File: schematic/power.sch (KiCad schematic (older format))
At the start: 21 parts, among them J1 Conn_01x02, J2 Conn_01x02, J3 Conn_01x02, J4 Conn_01x02, J5 Conn_02x06_Odd_Even, U1 LM2595S-3.3, U2 INA219AxD

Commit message: correct power D1, C1, C2 and L1 footprint. accurate L1, D1 and C2 values
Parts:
- D1: footprint Diode_SMD:D_0805_2012Metric_Castellated -> Diode_THT:D_DO-201AD_P15.24mm_Horizontal
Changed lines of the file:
@@
 F 0 "D1" V 5954 4679 50  0000 L CNN
 F 1 "D" V 6045 4679 50  0000 L CNN
-F 2 "Diode_SMD:D_0805_2012Metric_Castellated" H 6000 4600 50  0001 C CNN
+F 2 "Diode_THT:D_DO-201AD_P15.24mm_Horizontal" H 6000 4600 50  0001 C CNN
 F 3 "~" H 6000 4600 50  0001 C CNN
 	1    6000 4600

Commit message: added version
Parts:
- removed C1: C680uF, Capacitor_SMD:C_0805_2012Metric_Pad1.15x1.40mm_HandSolder, symbol Device:C
- removed C2: C220uF, Capacitor_SMD:C_0805_2012Metric_Pad1.15x1.40mm_HandSolder, symbol Device:C
- added C1, C2: 220uF, Capacitor_THT:CP_Radial_D8.0mm_P5.00mm, symbol Device:CP
- D1: value D -> 1N5822
- L1: value L33uH -> 68uH; footprint Inductor_SMD:L_1206_3216Metric_Pad1.42x1.75mm_HandSolder -> Inductor_SMD:L_Wuerth_WE-PD-Typ-7345
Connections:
- net +12V: now also C1.1
- net +3V3: now also C2.1
- net GND: now also C1.2, C2.2
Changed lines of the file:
@@
-	1    0    0    -1
-$EndComp
-$Comp
-L Device:C C2
-U 1 1 5EEDDF18
-P 6600 4600
-AR Path="/5EEDDF18" Ref="C2"  Part="1"
-AR Path="/5EEC6D97/5EEDDF18" Ref="C5"  Part="1"
-F 0 "C2" H 6715 4646 50  0000 L CNN
-F 1 "C220uF" H 6715 4555 50  0000 L CNN
-F 2 "Capacitor_SMD:C_0805_2012Metric_Pad1.15x1.40mm_HandSolder" H 6638 4450 50  0001 C CNN
-F 3 "~" H 6600 4600 50  0001 C CNN
-	1    6600 4600
-	1    0    0    -1
-$EndComp
-$Comp
-L Device:C C1
-U 1 1 5EEDDF1E
-P 4150 4400
-AR Path="/5EEDDF1E" Ref="C1"  Part="1"
-AR Path="/5EEC6D97/5EEDDF1E" Ref="C4"  Part="1"
-F 0 "C1" H 4265 4446 50  0000 L CNN
-F 1 "C680uF" H 4265 4355 50  0000 L CNN
-F 2 "Capacitor_SMD:C_0805_2012Metric_Pad1.15x1.40mm_HandSolder" H 4188 4250 50  0001 C CNN
-F 3 "~" H 4150 4400 50  0001 C CNN
-	1    4150 4400
 	1    0    0    -1
 $EndComp
@@
 AR Path="/5EEC6D97/5EEDDF32" Ref="D1"  Part="1"
 F 0 "D1" V 5954 4679 50  0000 L CNN
-F 1 "D" V 6045 4679 50  0000 L CNN
+F 1 "1N5822" V 6045 4679 50  0000 L CNN
 F 2 "Diode_THT:D_DO-201AD_P15.24mm_Horizontal" H 6000 4600 50  0001 C CNN
 F 3 "~" H 6000 4600 50  0001 C CNN
@@
 AR Path="/5EEC6D97/5EEDDF38" Ref="L1"  Part="1"
 F 0 "L1" V 6440 4450 50  0000 C CNN
-F 1 "L33uH" V 6349 4450 50  0000 C CNN
-F 2 "Inductor_SMD:L_1206_3216Metric_Pad1.42x1.75mm_HandSolder" H 6250 4450 50  0001 C CNN
+F 1 "68uH" V 6349 4450 50  0000 C CNN
+F 2 "Inductor_SMD:L_Wuerth_WE-PD-Typ-7345" H 6250 4450 50  0001 C CNN
 F 3 "~" H 6250 4450 50  0001 C CNN
 	1    6250 4450
@@
 Wire Wire Line
 	3600 4550 4150 4550
-Connection ~ 4150 4550
 $Comp
 L Connector_Generic:Conn_01x02 J1
@@
 Wire Wire Line
 	3400 4250 4150 4250
+$Comp
+L Device:CP C2
+U 1 1 5F0E578E
+P 6600 4600
+F 0 "C2" H 6718 4646 50  0000 L CNN
+F 1 "220uF" H 6718 4555 50  0000 L CNN
+F 2 "Capacitor_THT:CP_Radial_D8.0mm_P5.00mm" H 6638 4450 50  0001 C CNN
+F 3 "https://datasheet.octopart.com/EEUFM1V221L-Panasonic-datasheet-13266715.pdf" H 6600 4600 50  0001 C CNN
+F 4 "35" H 6600 4600 50  0001 C CNN "volt"
+	1    6600 4600
+	1    0    0    -1
+$EndComp
+$Comp
+L Device:CP C1
+U 1 1 5F0ECFE3
+P 4150 4400
+F 0 "C1" H 4268 4446 50  0000 L CNN
+F 1 "220uF" H 4268 4355 50  0000 L CNN
+F 2 "Capacitor_THT:CP_Radial_D8.0mm_P5.00mm" H 4188 4250 50  0001 C CNN
+F 3 "~" H 4150 4400 50  0001 C CNN
+	1    4150 4400
+	1    0    0    -1
+$EndComp
+Connection ~ 4150 4550
 $EndSCHEMATC

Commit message: added MPN
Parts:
- C3: MPN (none) -> C0805C106K8PACTU
- C4, C5: MPN (none) -> C0805C104J5RACTU
- D1: MPN (none) -> 1N5822
- L1: footprint Inductor_SMD:L_Wuerth_WE-PD-Typ-7345 -> Inductor_THT:L_Radial_L16.1mm_W16.1mm_Px7.62mm_Py12.70mm_Pulse_LP-44; MPN (none) -> PE-53830NL
- R1, R3: MPN (none) -> ERJ-P06J100V
- R2: footprint Resistor_SMD:R_4020_10251Metric_Pad1.65x5.30mm_HandSolder -> Resistor_SMD:R_2512_6332Metric_Pad1.52x3.35mm_HandSolder; MPN (none) -> CSNL2512FT1L00
- R4, R5: MPN (none) -> ERA-6AEB103V
- U2: MPN (none) -> INA219AIDR
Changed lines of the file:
@@
 F 2 "Diode_THT:D_DO-201AD_P15.24mm_Horizontal" H 6000 4600 50  0001 C CNN
 F 3 "~" H 6000 4600 50  0001 C CNN
+F 4 "1N5822" V 6000 4600 50  0001 C CNN "MPN"
 	1    6000 4600
 	0    1    1    0
@@
 F 0 "L1" V 6440 4450 50  0000 C CNN
 F 1 "68uH" V 6349 4450 50  0000 C CNN
-F 2 "Inductor_SMD:L_Wuerth_WE-PD-Typ-7345" H 6250 4450 50  0001 C CNN
+F 2 "Inductor_THT:L_Radial_L16.1mm_W16.1mm_Px7.62mm_Py12.70mm_Pulse_LP-44" H 6250 4450 50  0001 C CNN
 F 3 "~" H 6250 4450 50  0001 C CNN
+F 4 "PE-53830NL " V 6250 4450 50  0001 C CNN "MPN"
 	1    6250 4450
 	0    -1   -1   0
@@
 F 0 "R2" V 3043 4000 50  0000 C CNN
 F 1 "1m" V 3134 4000 50  0000 C CNN
-F 2 "Resistor_SMD:R_4020_10251Metric_Pad1.65x5.30mm_HandSolder" V 3180 4000 50  0001 C CNN
+F 2 "Resistor_SMD:R_2512_6332Metric_Pad1.52x3.35mm_HandSolder" V 3180 4000 50  0001 C CNN
 F 3 "~" H 3250 4000 50  0001 C CNN
+F 4 "CSNL2512FT1L00" V 3250 4000 50  0001 C CNN "MPN"
 	1    3250 4000
 	0    1    1    0
@@
 F 2 "Capacitor_SMD:C_0805_2012Metric_Pad1.15x1.40mm_HandSolder" H 3288 3450 50  0001 C CNN
 F 3 "~" H 3250 3600 50  0001 C CNN
+F 4 "C0805C104J5RACTU" V 3250 3600 50  0001 C CNN "MPN"
 	1    3250 3600
 	0    1    1    0
@@
 F 2 "Resistor_SMD:R_0805_2012Metric_Pad1.15x1.40mm_HandSolder" V 3030 3150 50  0001 C CNN
 F 3 "~" H 3100 3150 50  0001 C CNN
+F 4 "ERJ-P06J100V" H 3100 3150 50  0001 C CNN "MPN"
 	1    3100 3150
 	1    0    0    -1
@@
 F 2 "Resistor_SMD:R_0805_2012Metric_Pad1.15x1.40mm_HandSolder" V 3330 3150 50  0001 C CNN
 F 3 "~" H 3400 3150 50  0001 C CNN
+F 4 "ERJ-P06J100V" H 3400 3150 50  0001 C CNN "MPN"
 	1    3400 3150
 	1    0    0    -1
@@
 F 2 "Capacitor_SMD:C_0805_2012Metric_Pad1.15x1.40mm_HandSolder" H 2588 2200 50  0001 C CNN
 F 3 "~" H 2550 2350 50  0001 C CNN
+F 4 "C0805C106K8PACTU" V 2550 2350 50  0001 C CNN "MPN"
 	1    2550 2350
 	0    1    1    0
@@
 F 2 "Capacitor_SMD:C_0805_2012Metric_Pad1.15x1.40mm_HandSolder" H 2588 2650 50  0001 C CNN
 F 3 "~" H 2550 2800 50  0001 C CNN
+F 4 "C0805C104J5RACTU" V 2550 2800 50  0001 C CNN "MPN"
 	1    2550 2800
 	0    1    1    0
@@
 F 2 "Resistor_SMD:R_0805_2012Metric_Pad1.15x1.40mm_HandSolder" V 4280 2050 50  0001 C CNN
 F 3 "~" H 4350 2050 50  0001 C CNN
+F 4 "ERA-6AEB103V" H 4350 2050 50  0001 C CNN "MPN"
 	1    4350 2050
 	1    0    0    -1
@@
 F 2 "Resistor_SMD:R_0805_2012Metric_Pad1.15x1.40mm_HandSolder" V 4730 2050 50  0001 C CNN
 F 3 "~" H 4800 2050 50  0001 C CNN
+F 4 "ERA-6AEB103V" H 4800 2050 50  0001 C CNN "MPN"
 	1    4800 2050
 	1    0    0    -1
@@
 F 2 "Package_SO:SOIC-8_3.9x4.9mm_P1.27mm" H 4050 2150 50  0001 C CNN
 F 3 "http://www.ti.com/lit/ds/symlink/ina219.pdf" H 3600 2400 50  0001 C CNN
+F 4 "INA219AIDR" V 3250 2500 50  0001 C CNN "MPN"
 	1    3250 2500
 	0    -1   -1   0

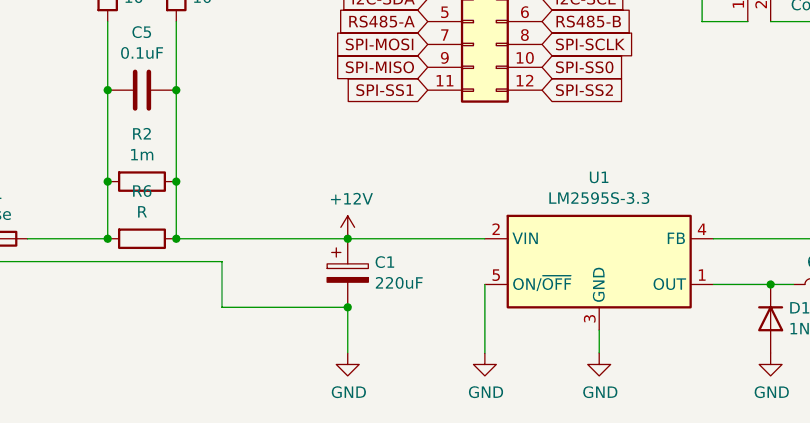
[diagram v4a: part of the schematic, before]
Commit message: added MPN for connectors
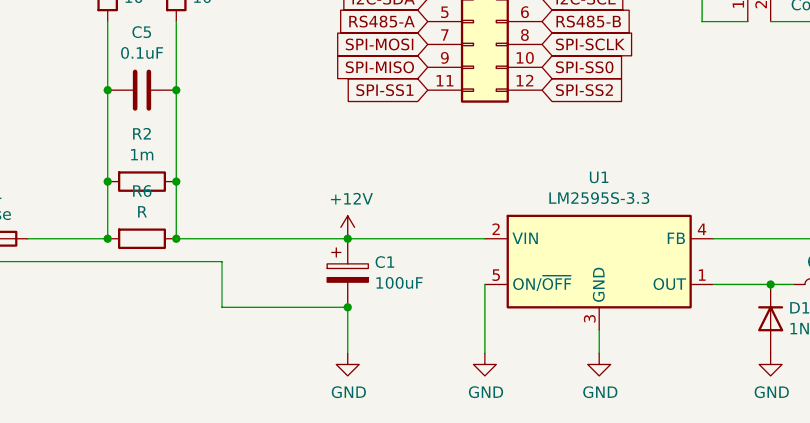
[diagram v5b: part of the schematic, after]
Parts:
- C1: value 220uF -> 100uF; footprint Capacitor_THT:CP_Radial_D8.0mm_P5.00mm -> Capacitor_THT:CP_Radial_D10.0mm_P5.00mm; MPN (none) -> EEUTP1V101
- C2: footprint Capacitor_THT:CP_Radial_D8.0mm_P5.00mm -> Capacitor_THT:CP_Radial_D8.0mm_P3.50mm; MPN (none) -> ESW227M035AG4AA; volt 35 -> (none)
- J1, J2, J3, J4: MPN (none) -> PRT-10474
- J5: MPN (none) -> BHR-12-VUA
- U1: MPN (none) -> LM2595S-3.3/NOPB
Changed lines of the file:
@@
 F 2 "Package_TO_SOT_SMD:TO-263-5_TabPin3" H 5300 4100 50  0001 L CIN
 F 3 "http://www.ti.com.cn/cn/lit/ds/symlink/lm2595.pdf" H 5250 4350 50  0001 C CNN
+F 4 "LM2595S-3.3/NOPB" H 5250 4350 50  0001 C CNN "MPN"
 	1    5250 4350
 	1    0    0    -1
@@
 F 2 "Connector_AMASS:AMASS_XT60-M_1x02_P7.20mm_Vertical" H 2250 4350 50  0001 C CNN
 F 3 "~" H 2250 4350 50  0001 C CNN
+F 4 "PRT-10474" H 2250 4350 50  0001 C CNN "MPN"
 	1    2250 4350
 	-1   0    0    1
@@
 F 2 "Connector_AMASS:AMASS_XT60-F_1x02_P7.20mm_Vertical" H 5900 2300 50  0001 C CNN
 F 3 "~" H 5900 2300 50  0001 C CNN
+F 4 "PRT-10474" V 5900 2300 50  0001 C CNN "MPN"
 	1    5900 2300
 	0    -1   -1   0
@@
 F 2 "Connector_AMASS:AMASS_XT60-F_1x02_P7.20mm_Vertical" H 5900 2700 50  0001 C CNN
 F 3 "~" H 5900 2700 50  0001 C CNN
+F 4 "PRT-10474" V 5900 2700 50  0001 C CNN "MPN"
 	1    5900 2700
 	0    -1   -1   0
@@
 F 2 "Connector_AMASS:AMASS_XT60-F_1x02_P7.20mm_Vertical" H 5900 3100 50  0001 C CNN
 F 3 "~" H 5900 3100 50  0001 C CNN
+F 4 "PRT-10474" V 5900 3100 50  0001 C CNN "MPN"
 	1    5900 3100
 	0    -1   -1   0
@@
 F 2 "Connector_IDC:IDC-Header_2x06_P2.54mm_Vertical" H 4700 3300 50  0001 C CNN
 F 3 "~" H 4700 3300 50  0001 C CNN
+F 4 "BHR-12-VUA" H 4700 3300 50  0001 C CNN "MPN"
 	1    4700 3300
 	1    0    0    -1
@@
 F 0 "C2" H 6718 4646 50  0000 L CNN
 F 1 "220uF" H 6718 4555 50  0000 L CNN
-F 2 "Capacitor_THT:CP_Radial_D8.0mm_P5.00mm" H 6638 4450 50  0001 C CNN
-F 3 "https://datasheet.octopart.com/EEUFM1V221L-Panasonic-datasheet-13266715.pdf" H 6600 4600 50  0001 C CNN
-F 4 "35" H 6600 4600 50  0001 C CNN "volt"
+F 2 "Capacitor_THT:CP_Radial_D8.0mm_P3.50mm" H 6638 4450 50  0001 C CNN
+F 3 "~" H 6600 4600 50  0001 C CNN
+F 4 "ESW227M035AG4AA" H 6600 4600 50  0001 C CNN "MPN"
 	1    6600 4600
 	1    0    0    -1
@@
 P 4150 4400
 F 0 "C1" H 4268 4446 50  0000 L CNN
-F 1 "220uF" H 4268 4355 50  0000 L CNN
-F 2 "Capacitor_THT:CP_Radial_D8.0mm_P5.00mm" H 4188 4250 50  0001 C CNN
+F 1 "100uF" H 4268 4355 50  0000 L CNN
+F 2 "Capacitor_THT:CP_Radial_D10.0mm_P5.00mm" H 4188 4250 50  0001 C CNN
 F 3 "~" H 4150 4400 50  0001 C CNN
+F 4 "EEUTP1V101" H 4150 4400 50  0001 C CNN "MPN"
 	1    4150 4400
 	1    0    0    -1
